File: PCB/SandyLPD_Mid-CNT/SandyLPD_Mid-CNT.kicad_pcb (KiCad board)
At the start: 2 copper layers, 49.4 x 61 mm, 45 parts

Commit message: シルク位置調整 #20
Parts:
- moved REF** 2.52 mm to (150.8, 62.7)
- moved REF** 2.45 mm to (150.8, 62.5)
- moved REF** 1.98 mm to (151.4, 72.7)
- moved REF** 1.88 mm to (151.4, 72.8)
- moved REF** 1.86 mm to (150.8, 45.7)
- moved REF** 1.77 mm to (150.8, 45.5)
- moved REF** 1.38 mm to (152.4, 85.8)
- moved REF** 1.04 mm to (152.3, 85.5)
- turned T_R0 to 0 degrees
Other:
- board text added: "L Back"
- board text added: "R Back"
- board text removed: "L 左 Back"
- board text removed: "R 右 Back"
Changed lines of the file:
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@@
 		(locked yes)
 		(layer "F.Cu")
-		(at 152.664851 45.783915)
+		(at 150.803908 45.744852)
 		(property "Reference" "REF**"
 			(at 0 0.5 0)
@@
 		(locked yes)
 		(layer "F.Cu")
-		(at 153.217912 73.437806)
+		(at 151.379269 72.691759)
 		(property "Reference" "REF**"
 			(at 0 -0.5 0)
@@
 		(locked yes)
 		(layer "F.Cu")
-		(at 153.260164 63.047992)
+		(at 150.761661 62.739432)
 		(property "Reference" "REF**"
 			(at 0 0.5 0)
@@
 		(locked yes)
 		(layer "F.Cu")
-		(at 153.725917 85.537615)
+		(at 152.377287 85.821784)
 		(property "Reference" "REF**"
 			(at 0 0.5 0)
@@
 		(locked yes)
 		(layer "B.Cu")
-		(at 153.305222 85.537613 180)
+		(at 152.270744 85.479764 180)
 		(property "Reference" "REF**"
 			(at 0 -0.5 0)
@@
 		(locked yes)
 		(layer "B.Cu")
-		(at 153.217913 73.437808 180)
+		(at 151.431974 72.842495 180)
 		(property "Reference" "REF**"
 			(at 0 0.5 0)
@@
 		(locked yes)
 		(layer "B.Cu")
-		(at 152.580357 45.783915 180)
+		(at 150.836661 45.458097 180)
 		(property "Reference" "REF**"
 			(at 0 -0.5 0)
@@
 		(fp_arc
 			(start 0.7 3.345415)
-			(mid 0.662237 3.758478)
+			(mid 0.662236 3.758481)
 			(end 0.272339 3.9)
 			(stroke
@@
 		(locked yes)
 		(layer "B.Cu")
-		(at 153.17567 63.047992 180)
+		(at 150.794414 62.452677 180)
 		(property "Reference" "REF**"
 			(at 0 -0.5 0)
@@
 		(fp_arc
 			(start 0.7 3.345415)
-			(mid 0.662237 3.758478)
+			(mid 0.662236 3.758481)
 			(end 0.272339 3.9)
 			(stroke
@@
 	(footprint "locallib:TestPoint_THTPad_D2.0mm_Drill1.0mm"
 		(layer "B.Cu")
-		(at 134.167901 38.909656 180)
+		(at 134.167901 38.909656)
 		(descr "THT pad as test Point, diameter 2.0mm, hole diameter 1.0mm")
 		(tags "test point THT pad")
 		(property "Reference" "T_R0"
-			(at 0 1.998 0)
+			(at 0 1.998 360)
 			(layer "B.SilkS")
 			(effects
@@
 		)
 		(property "Value" "Conn_01x01"
-			(at 0 -2.05 0)
+			(at 0 -2.05 360)
 			(layer "B.Fab")
 			(effects
@@
 		)
 		(property "Footprint" "locallib:TestPoint_THTPad_D2.0mm_Drill1.0mm"
-			(at 0 0 0)
+			(at 0 0 180)
 			(unlocked yes)
 			(layer "B.Fab")
@@
 		)
 		(property "Datasheet" ""
-			(at 0 0 0)
+			(at 0 0 180)
 			(unlocked yes)
 			(layer "B.Fab")
@@
 		)
 		(property "Description" ""
-			(at 0 0 0)
+			(at 0 0 180)
 			(unlocked yes)
 			(layer "B.Fab")
@@
 		)
 		(fp_text user "${REFERENCE}"
-			(at 0 2 0)
+			(at 0 2 360)
 			(layer "B.Fab")
 			(effects
@@
 		)
 		(pad "1" thru_hole circle
-			(at 0 0 180)
+			(at 0 0)
 			(size 2 2)
 			(drill 1)
@@
 		(fp_arc
 			(start 0.7 3.345415)
-			(mid 0.662236 3.758481)
+			(mid 0.662237 3.758478)
 			(end 0.272339 3.9)
 			(stroke
@@
 	)
 	(gr_rect
-		(start 127.220935 64.80028)
-		(end 132.220935 69.80028)
+		(start 127.608435 64.80028)
+		(end 132.608435 69.80028)
 		(stroke
 			(width 0.3)
@@
 	)
 	(gr_rect
-		(start 108.220935 45.60028)
-		(end 113.220935 50.60028)
+		(start 108.608435 45.60028)
+		(end 113.608435 50.60028)
 		(stroke
 			(width 0.3)
@@
 	)
 	(gr_rect
-		(start 136.795935 83.80028)
-		(end 141.795935 88.80028)
+		(start 137.158435 83.80028)
+		(end 142.158435 88.80028)
 		(stroke
 			(width 0.3)
@@
 	)
 	(gr_rect
-		(start 127.195935 64.80028)
-		(end 132.195935 69.80028)
+		(start 127.583435 64.80028)
+		(end 132.583435 69.80028)
 		(stroke
 			(width 0.3)
@@
 	)
 	(gr_rect
-		(start 136.820935 83.80028)
-		(end 141.820935 88.80028)
+		(start 137.183435 83.80028)
+		(end 142.183435 88.80028)
 		(stroke
 			(width 0.3)
@@
 	)
 	(gr_rect
-		(start 108.195935 45.60028)
-		(end 113.195935 50.60028)
+		(start 108.583435 45.60028)
+		(end 113.583435 50.60028)
 		(stroke
 			(width 0.3)
@@
 		(layer "F.SilkS")
 	)
-	(gr_text "L 左 Back"
-		(at 142.983435 38.70028 0)
+	(gr_text "L Back"
+		(at 133.483435 49.30028 90)
 		(layer "B.SilkS" knockout)
 		(effects
 			(font
-				(size 1.8 1.8)
+				(size 2 2)
 				(thickness 0.24)
 				(italic yes)
@@
 	)
 	(gr_text "#SandyLP_Duo DN0010"
-		(at 149.183435 40.30028 90)
+		(at 147.783435 40.10028 90)
 		(layer "B.SilkS")
 		(effects
@@
 		)
 	)
-	(gr_text "R 右 Back"
-		(at 142.583435 38.60028 0)
+	(gr_text "R Back"
+		(at 133.383435 49.70028 90)
 		(layer "F.SilkS" knockout)
 		(effects
 			(font
-				(size 1.8 1.8)
+				(size 2 2)
 				(thickness 0.24)
 				(italic yes)

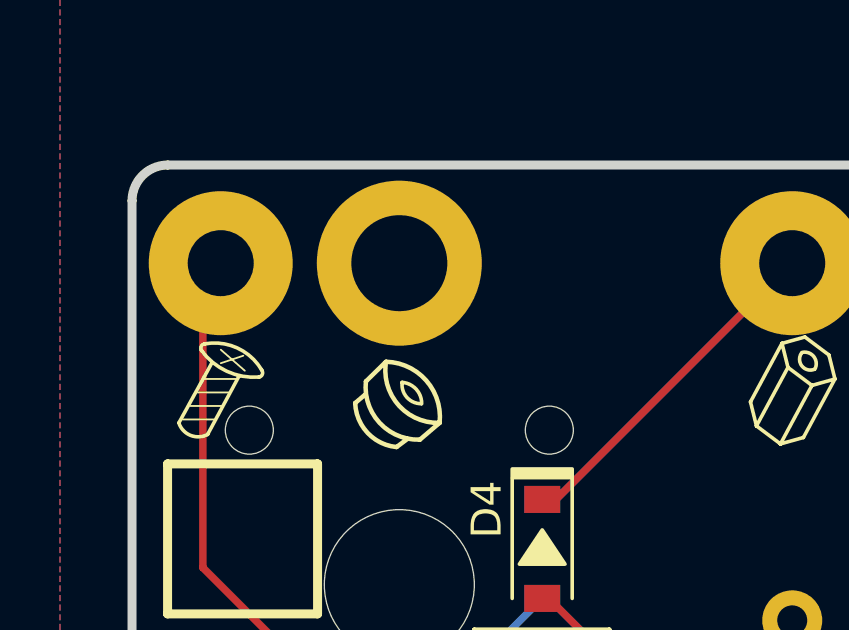
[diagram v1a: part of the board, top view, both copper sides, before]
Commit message: Mid-CNTのプレート固定用スルーホールタップを1個減らす
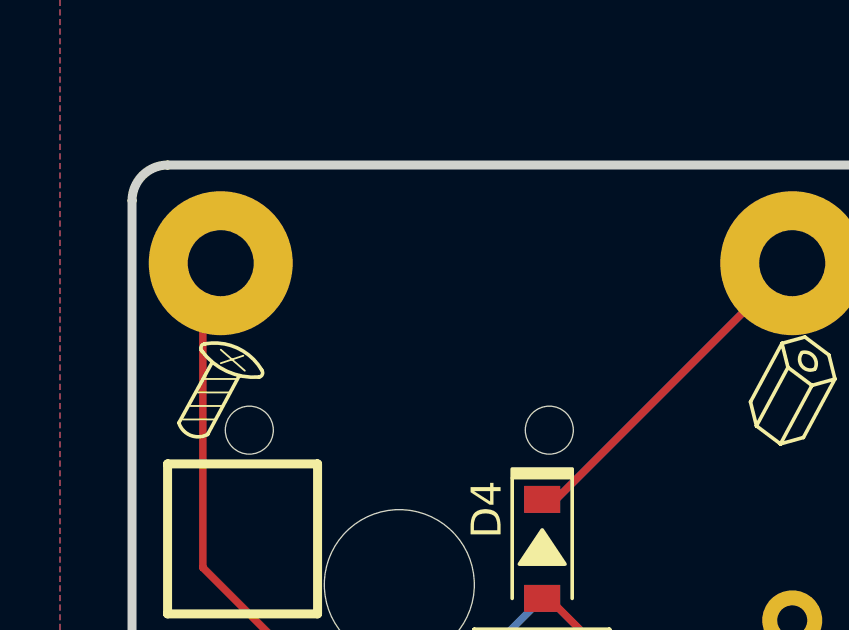
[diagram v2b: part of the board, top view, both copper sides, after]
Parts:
- removed the H5 at (116.3, 38.9)
- removed the REF** at (116.3, 43.7) (x2)
- renumbered H6 to H5

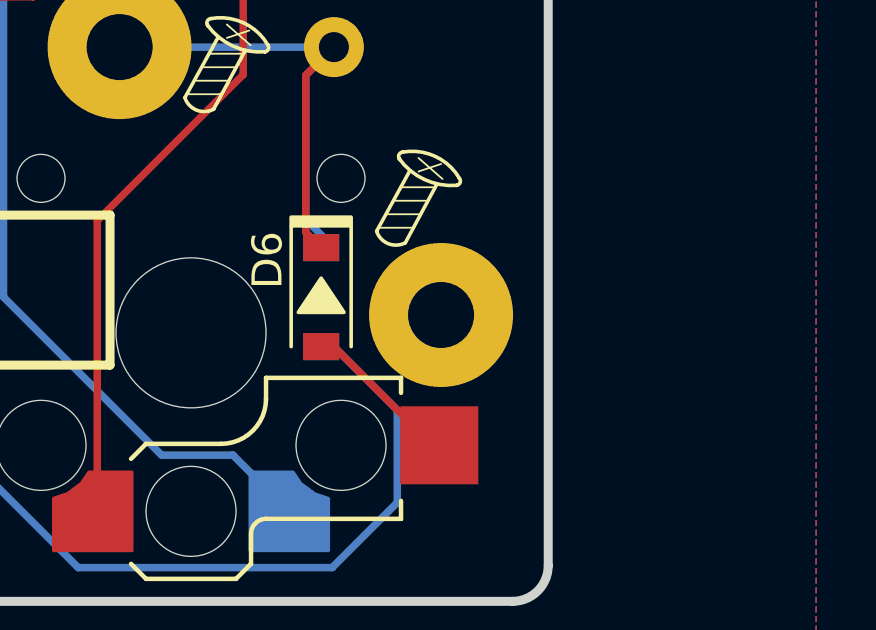
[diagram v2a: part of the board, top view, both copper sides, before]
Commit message: スイッチにネジ頭がかかるため、基板Baseと基板Mid-CNTを接続するネジ位置を調整。
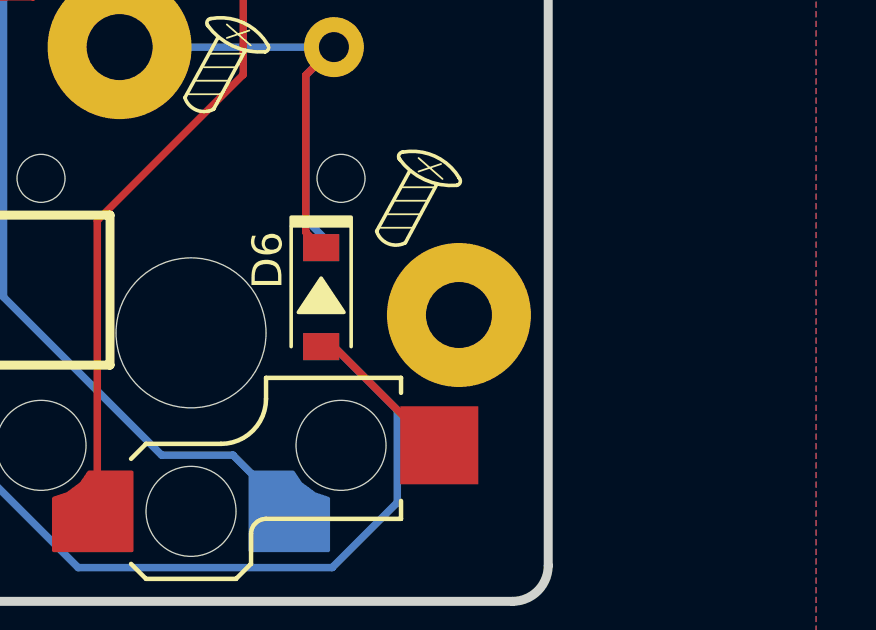
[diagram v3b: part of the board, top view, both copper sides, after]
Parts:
- H1, H2, H3, H4: footprint locallib:MountingHole_2.2-4.8mm_M2_Pad_minimal_for_Through-hole_tap -> locallib:MountingHole_2.2-4.8mm_M2_Pad_minimal_for_Through-hole_tap_L3mm
- moved H4 0.60 mm to (153.8, 87.1)
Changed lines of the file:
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@@
 	(net 11 "Mid_row0")
 	(net 12 "GND")
-	(footprint "locallib:MountingHole_2.2-4.8mm_M2_Pad_minimal_for_Through-hole_tap"
+	(footprint "locallib:MountingHole_2.2-4.8mm_M2_Pad_minimal_for_Through-hole_tap_L3mm"
 		(layer "F.Cu")
-		(at 153.217917 87.130009)
+		(at 153.813226 87.130009)
 		(descr "Mounting Hole 2.2mm, M2")
 		(tags "mounting hole 2.2mm m2")
@@
 			)
 		)
-		(property "Footprint" "locallib:MountingHole_2.2-4.8mm_M2_Pad_minimal_for_Through-hole_tap"
+		(property "Footprint" "locallib:MountingHole_2.2-4.8mm_M2_Pad_minimal_for_Through-hole_tap_L3mm"
 			(at 0 0 0)
 			(layer "F.Fab")
@@
 			(pintype "input")
 		)
+		(model "${KIPRJMOD}/locallib.pretty/Screw-M2-3mm-SlimHead.step"
+			(offset
+				(xyz 0 0 0)
+			)
+			(scale
+				(xyz 1 1 1)
+			)
+			(rotate
+				(xyz 0 -90 0)
+			)
+		)
 	)
 	(footprint "locallib:ICON_Screw_Medium"
@@
 		)
 	)
-	(footprint "locallib:MountingHole_2.2-4.8mm_M2_Pad_minimal_for_Through-hole_tap"
+	(footprint "locallib:MountingHole_2.2-4.8mm_M2_Pad_minimal_for_Through-hole_tap_L3mm"
 		(layer "F.Cu")
 		(at 129.40531 59.15028)
@@
 			)
 		)
-		(property "Footprint" "locallib:MountingHole_2.2-4.8mm_M2_Pad_minimal_for_Through-hole_tap"
+		(property "Footprint" "locallib:MountingHole_2.2-4.8mm_M2_Pad_minimal_for_Through-hole_tap_L3mm"
 			(at 0 0 0)
 			(layer "F.Fab")
@@
 			(pintype "input")
 		)
+		(model "${KIPRJMOD}/locallib.pretty/Screw-M2-3mm-SlimHead.step"
+			(offset
+				(xyz 0 0 0)
+			)
+			(scale
+				(xyz 1 1 1)
+			)
+			(rotate
+				(xyz 0 -90 0)
+			)
+		)
 	)
 	(footprint "locallib:SandyLPD_outline_Mid-CNT"
@@
 		)
 	)
-	(footprint "locallib:MountingHole_2.2-4.8mm_M2_Pad_minimal_for_Through-hole_tap"
+	(footprint "locallib:MountingHole_2.2-4.8mm_M2_Pad_minimal_for_Through-hole_tap_L3mm"
 		(layer "F.Cu")
 		(at 110.355381 38.909656)
@@
 			)
 		)
-		(property "Footprint" "locallib:MountingHole_2.2-4.8mm_M2_Pad_minimal_for_Through-hole_tap"
+		(property "Footprint" "locallib:MountingHole_2.2-4.8mm_M2_Pad_minimal_for_Through-hole_tap_L3mm"
 			(at 0 0 0)
 			(layer "F.Fab")
@@
 			(pintype "input")
 		)
+		(model "${KIPRJMOD}/locallib.pretty/Screw-M2-3mm-SlimHead.step"
+			(offset
+				(xyz 0 0 0)
+			)
+			(scale
+				(xyz 1 1 1)
+			)
+			(rotate
+				(xyz 0 -90 0)
+			)
+		)
 	)
 	(footprint "locallib:Kailh_socket_ChocV2_small_#2pad_for_Reverse_no_hole"
@@
 		)
 	)
-	(footprint "locallib:MountingHole_2.2-4.8mm_M2_Pad_minimal_for_Through-hole_tap"
+	(footprint "locallib:MountingHole_2.2-4.8mm_M2_Pad_minimal_for_Through-hole_tap_L3mm"
 		(layer "F.Cu")
 		(at 142.502283 78.200314)
@@
 			)
 		)
-		(property "Footprint" "locallib:MountingHole_2.2-4.8mm_M2_Pad_minimal_for_Through-hole_tap"
+		(property "Footprint" "locallib:MountingHole_2.2-4.8mm_M2_Pad_minimal_for_Through-hole_tap_L3mm"
 			(at 0 0 0)
 			(layer "F.Fab")
@@
 			(pintype "input")
 		)
+		(model "${KIPRJMOD}/locallib.pretty/Screw-M2-3mm-SlimHead.step"
+			(offset
+				(xyz 0 0 0)
+			)
+			(scale
+				(xyz 1 1 1)
+			)
+			(rotate
+				(xyz 0 -90 0)
+			)
+		)
 	)
 	(footprint "locallib:ICON_Through-hole_Tap"
@@
 		(fp_arc
 			(start 0.7 3.345415)
-			(mid 0.662236 3.758481)
+			(mid 0.662237 3.758478)
 			(end 0.272339 3.9)
 			(stroke
@@
 		(fp_arc
 			(start 0.7 3.345415)
-			(mid 0.662236 3.758481)
+			(mid 0.662237 3.758478)
 			(end 0.272339 3.9)
 			(stroke
@@
 		(fp_arc
 			(start 0.7 3.345415)
-			(mid 0.662237 3.758478)
+			(mid 0.662236 3.758481)
 			(end 0.272339 3.9)
 			(stroke

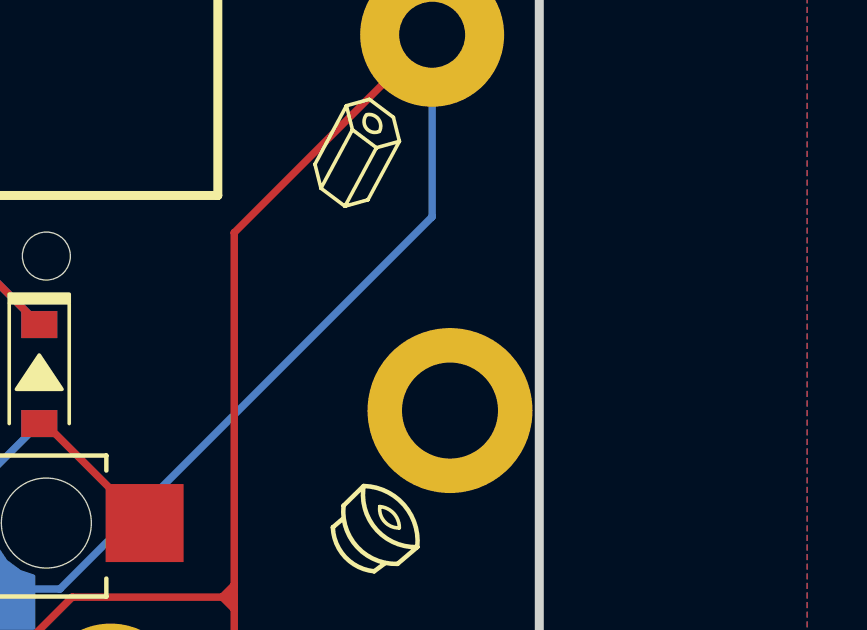
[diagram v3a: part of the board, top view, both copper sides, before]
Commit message: ネジ等の3Dモデル追加
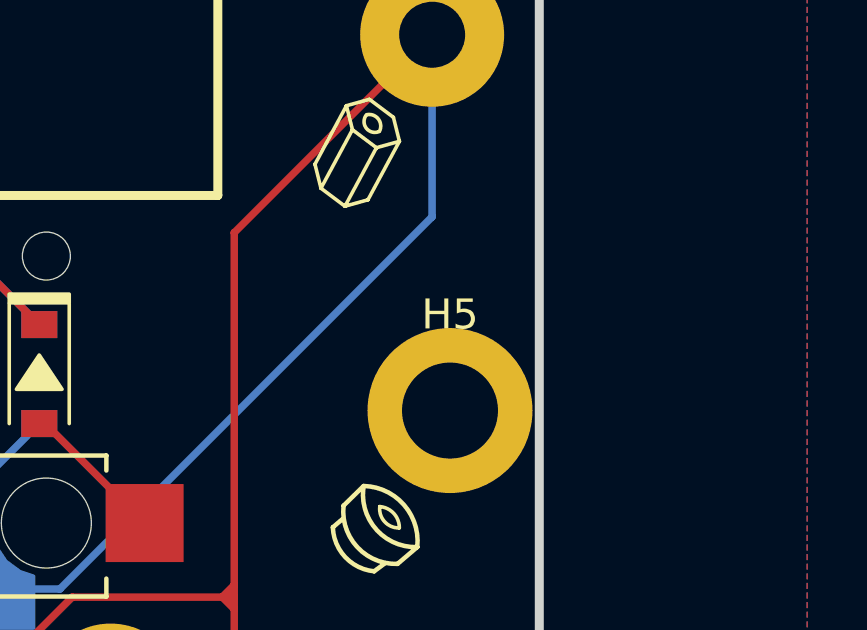
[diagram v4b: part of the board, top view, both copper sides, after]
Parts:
- H5: footprint locallib:MountingHole_M2_Through-hole_tap_THC-0.8-x-2 -> locallib:MountingHole_M2_Through-hole_tap_THC-0.8-1.0-2
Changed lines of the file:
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@@
 		)
 	)
-	(footprint "locallib:MountingHole_M2_Through-hole_tap_THC-0.8-x-2"
+	(footprint "locallib:MountingHole_M2_Through-hole_tap_THC-0.8-1.0-2"
 		(layer "F.Cu")
 		(at 153.81323 68.70032)
@@
 			(at 0 -3.2 0)
 			(layer "F.SilkS")
-			(hide yes)
 			(effects
 				(font
@@
 			)
 		)
-		(property "Footprint" "locallib:MountingHole_M2_Through-hole_tap_THC-0.8-x-2"
+		(property "Footprint" "locallib:MountingHole_M2_Through-hole_tap_THC-0.8-1.0-2"
 			(at 0 0 0)
 			(unlocked yes)
@@
 			(remove_unused_layers no)
 		)
+		(model "${KIPRJMOD}/locallib.pretty/ThroughHole-Tap_THC-0.8-1.0-2-Fusion.step"
+			(opacity 0.7500)
+			(offset
+				(xyz 0 0 0)
+			)
+			(scale
+				(xyz 1 1 1)
+			)
+			(rotate
+				(xyz 0 0 0)
+			)
+		)
 	)
 	(footprint "locallib:ICON_Spacer"
@@
 		(fp_arc
 			(start 0.7 3.345415)
-			(mid 0.662237 3.758478)
+			(mid 0.662236 3.758481)
 			(end 0.272339 3.9)
 			(stroke
@@
 		(fp_arc
 			(start 0.7 3.345415)
-			(mid 0.662237 3.758478)
+			(mid 0.662236 3.758481)
 			(end 0.272339 3.9)
 			(stroke
@@
 		(fp_arc
 			(start 0.7 3.345415)
-			(mid 0.662236 3.758481)
+			(mid 0.662237 3.758478)
 			(end 0.272339 3.9)
 			(stroke
